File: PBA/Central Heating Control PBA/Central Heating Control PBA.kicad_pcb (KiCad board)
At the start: 2 copper layers, 173.4 x 85.5 mm, 153 parts, among them J1 Screw_Terminal_01x03, J10 Screw_Terminal_01x02, J11 Screw_Terminal_01x02, J12 Screw_Terminal_01x02, J13 Screw_Terminal_01x02, J2 Conn_01x11, J3 Screw_Terminal_01x02, J3_DC5V1 Screw_Terminal_01x02, J4 Screw_Terminal_01x02, J4_AC_OUTPUT1 Screw_Terminal_01x02, J5 Screw_Terminal_01x02, J5_AC_INPUT1 Screw_Terminal_01x02, J6 Screw_Terminal_01x02, J7 Screw_Terminal_01x02, J8 Screw_Terminal_01x02, J9 Screw_Terminal_01x02, Q1 BT136-600, Q10 BT136-600, Q11 BC857, Q12 BC857, Q13 BC857, Q14 BC857, Q15 BC857, Q16 BC857, Q17 BC857, Q18 BC857, Q19 BC857, Q2 BT136-600, Q20 BC857, Q21 BC857, Q22 BT136-600, Q3 BT136-600, Q4 BT136-600, Q5 BT136-600, Q6 BT136-600, Q7 BT136-600, Q8 BT136-600, Q9 BT136-600, U1 ESP32_DevKit_V1_DOIT, U10 MOC3083M, U11 MOC3083M, U12 MOC3083M, U2 MOC3083M, U3 MOC3083M, U4 MOC3083M, U5 MOC3083M, U6 MOC3083M, U7 MOC3083M, U8 MOC3083M, U9 MOC3083M

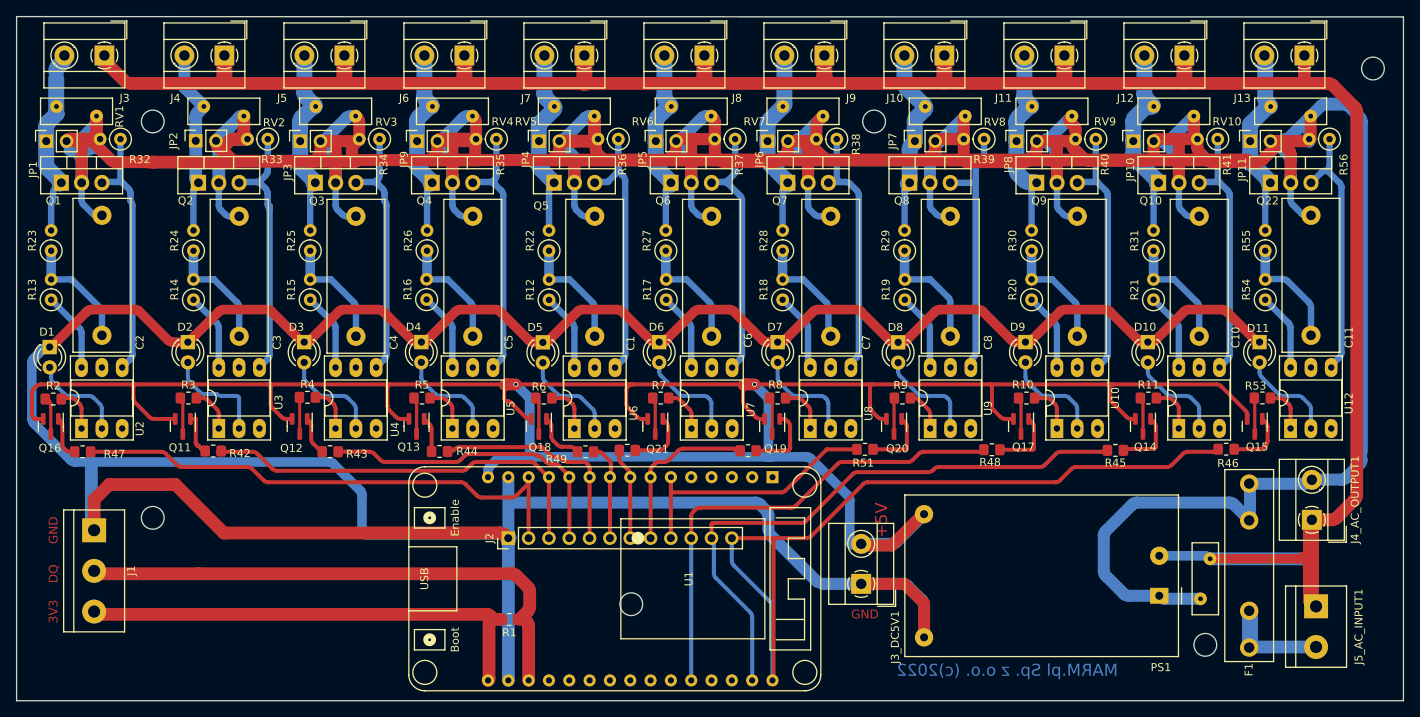
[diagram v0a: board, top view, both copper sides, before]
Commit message: Update PBA for DHT22 and footprints... Removed ArduinoJson adding getJsonVal function recuces about 4k of code for only read json value
Signed-off-by: rgw <rgw@marm.pl>
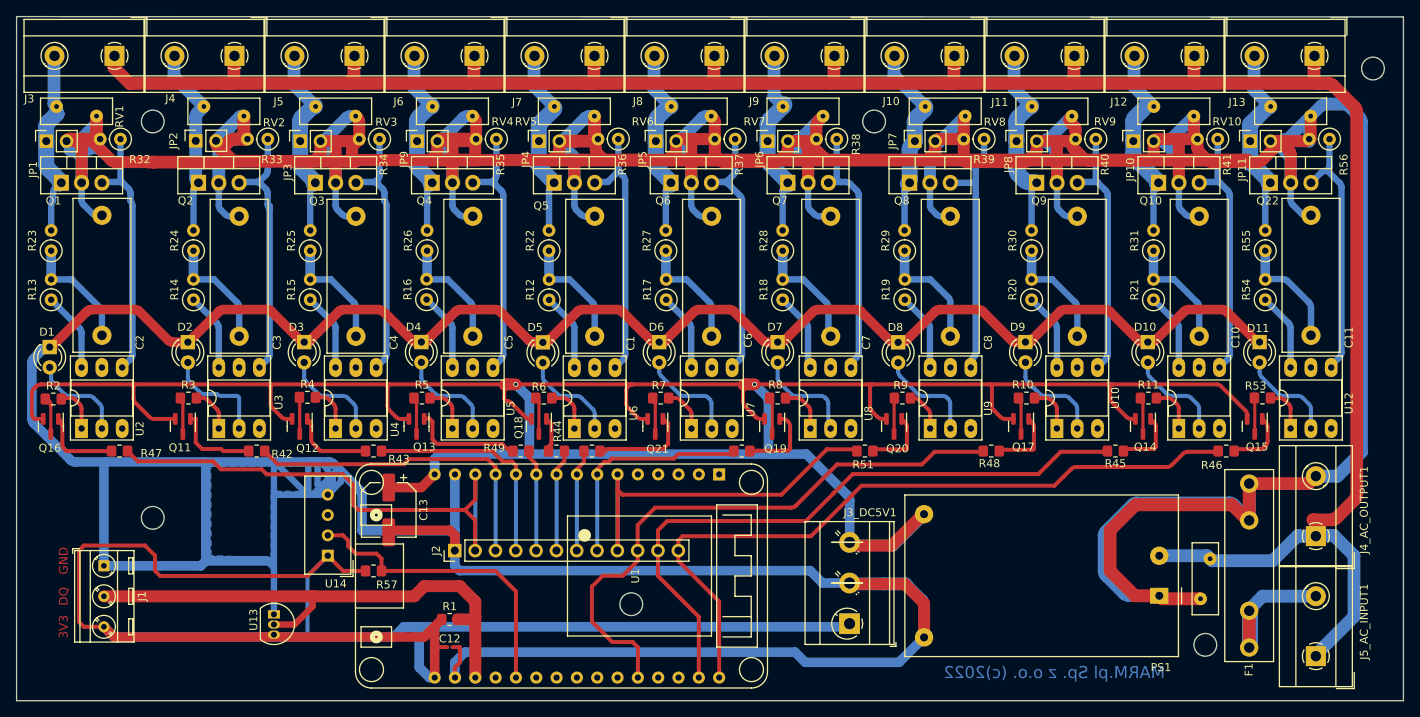
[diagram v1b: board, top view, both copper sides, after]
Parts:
- added C12: 10u 6.3, Capacitor_SMD:C_0201_0603Metric_Pad0.64x0.40mm_HandSolder, F.Cu at (87.6, 115.6)
- added C13: 100/16, Capacitor_SMD:CP_Elec_6.3x5.9, F.Cu at (80.0, 98.4)
- added R57: 10k, Resistor_SMD:R_0805_2012Metric_Pad1.20x1.40mm_HandSolder, F.Cu at (78.1, 106.0)
- added U13: DS18B20, Package_TO_SOT_THT:TO-92L_Inline, F.Cu at (65.7, 111.5)
- added U14: DHT11, Sensor:Aosong_DHT11_5.5x12.0_P2.54mm, F.Cu at (72.4, 104.1)
- J1: footprint TerminalBlock:TerminalBlock_bornier-3_P5.08mm -> TerminalBlock_MetzConnect:TerminalBlock_MetzConnect_Type086_RT03403HBLC_1x03_P3.81mm_Horizontal
- J10, J11, J12, J13, J3, J4, J4_AC_OUTPUT1, J5, J6, J7, J8, J9: footprint TerminalBlock_MetzConnect:TerminalBlock_MetzConnect_Type055_RT01502HDWU_1x02_P5.00mm_Horizontal -> TerminalBlock_MetzConnect:TerminalBlock_MetzConnect_Type171_RT13702HBWC_1x02_P7.50mm_Horizontal
- J3_DC5V1: footprint TerminalBlock_MetzConnect:TerminalBlock_MetzConnect_Type055_RT01502HDWU_1x02_P5.00mm_Horizontal -> TerminalBlock_MetzConnect:TerminalBlock_MetzConnect_Type073_RT02603HBLU_1x03_P5.08mm_Horizontal
- J5_AC_INPUT1: footprint TerminalBlock:TerminalBlock_bornier-2_P5.08mm -> TerminalBlock_MetzConnect:TerminalBlock_MetzConnect_Type171_RT13702HBWC_1x02_P7.50mm_Horizontal
- moved R44 10.2 mm to (96.5, 91.1)
- moved R1 7.46 mm to (87.6, 112.1)
- moved J2 6.87 mm to (88.3, 103.5)
- moved U1 6.68 mm to (121.3, 106.7)
- moved J5_AC_INPUT1 6.23 mm to (195.9, 116.7), turned to 90 degrees
- moved R42 5.43 mm to (63.5, 91.1)
- moved R43 5.42 mm to (78.1, 91.1)
- moved J3_DC5V1 5.18 mm to (137.6, 112.6)
- moved J1 4.61 mm to (44.4, 105.4)
- moved R47 4.61 mm to (46.4, 91.1)
- moved R52 4.42 mm to (105.4, 91.1)
- moved R49 3.65 mm to (101.0, 91.1)
- moved J4_AC_OUTPUT1 2.10 mm to (195.9, 101.7)
- moved J10 1.27 mm to (150.7, 41.7)
- moved J11 1.27 mm to (165.7, 41.7)
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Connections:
- J3_DC5V1 pad 1: GNDREF -> +3V3
- J3_DC5V1 pad 2: +5V -> GNDREF
- U1 pad 20: unconnected-(U1-Pad20) -> Net-(U1-Pad20)
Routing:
- net +3V3: track 60.0 -> 219.1 mm
- net GNDREF: track 433.4 -> 527.8 mm
- net Net-(C1-Pad2): track 778.9 -> 829.4 mm
- net Net-(U1-Pad20): track 0.00 -> 38.5 mm
- net NEUT: track 322.2 -> 295.5 mm
- net Net-(J2-Pad9): track 34.5 -> 51.6 mm
- net Net-(J2-Pad5): track 27.7 -> 12.8 mm
- net +5V: track 314.2 -> 329.1 mm
- net Net-(J2-Pad10): track 60.5 -> 73.7 mm
- net Net-(J2-Pad12): track 103.3 -> 91.4 mm
- net Net-(J2-Pad3): track 50.9 -> 40.7 mm
- net Net-(J2-Pad4): track 38.4 -> 28.2 mm
- net Net-(Q13-Pad1): track 4.41 -> 14.1 mm
- net Net-(J2-Pad8): track 20.9 -> 28.2 mm
- net Net-(J2-Pad11): track 73.8 -> 80.6 mm
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- added copper zone on B.Cu, net GNDREF
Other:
- board text added: "3V3 GND 5V"
- board text removed: "+5V"
- board text removed: "GND 5V"
